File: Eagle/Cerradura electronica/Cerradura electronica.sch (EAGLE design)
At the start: 37 parts, among them IC1 LD117AS50TR, Q1 2N3904, Q2 IRF540N

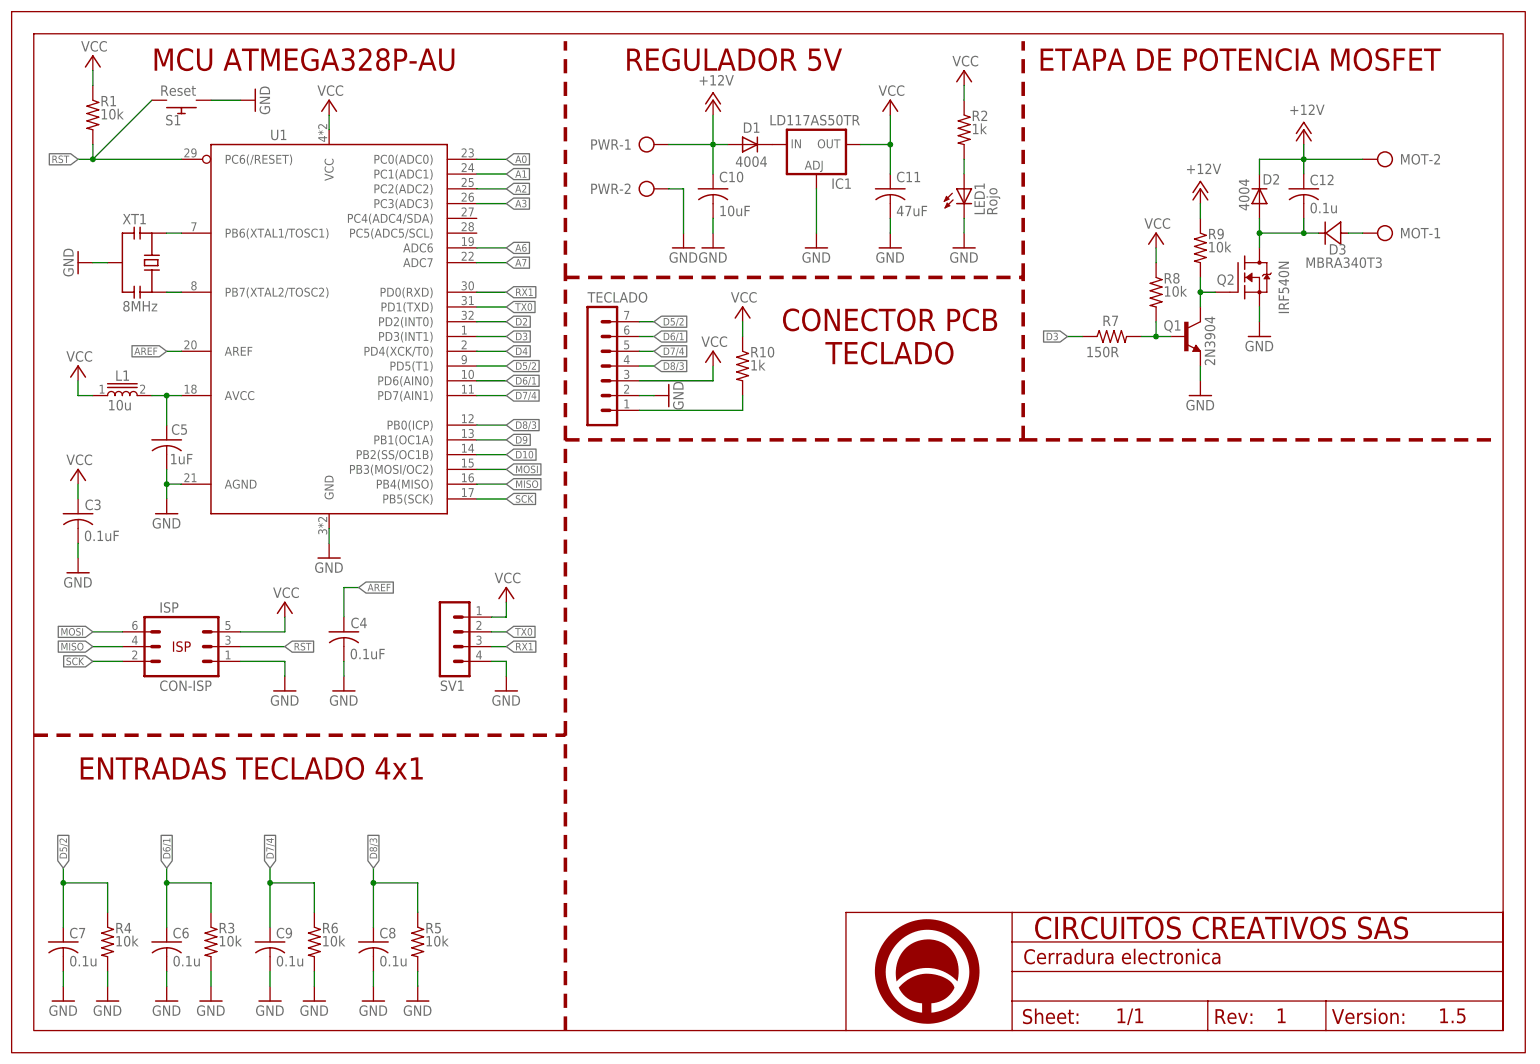
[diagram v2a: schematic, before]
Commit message: Add BUZZER para mejorar la funcionalidad, terminado v1.5.1
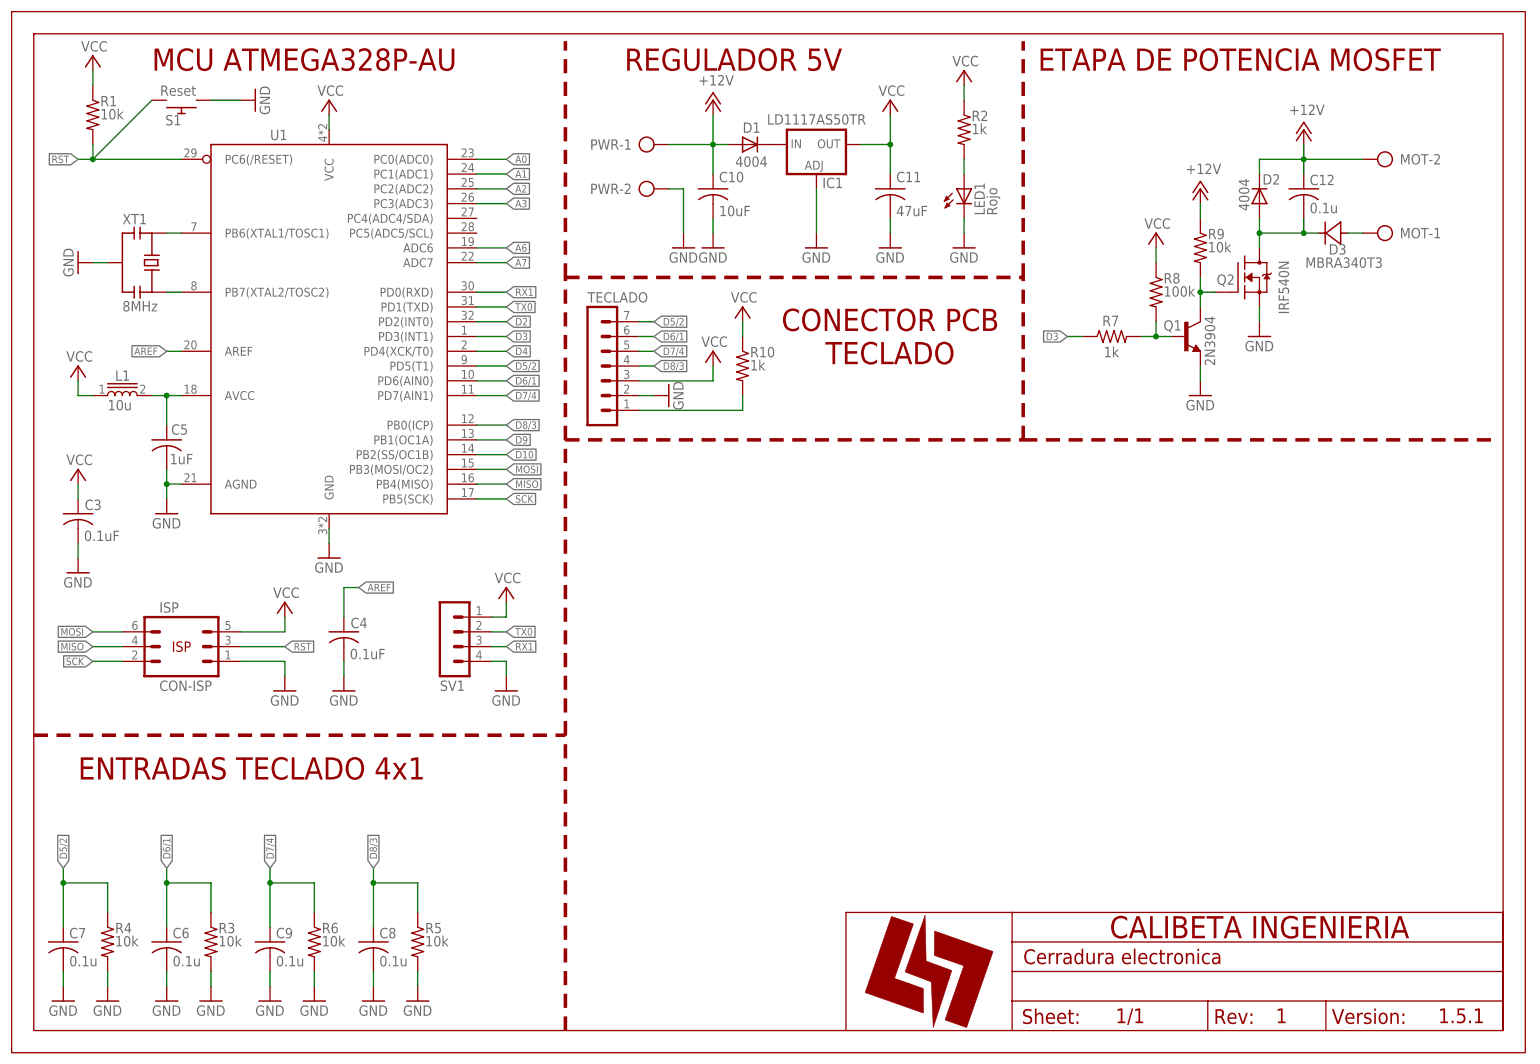
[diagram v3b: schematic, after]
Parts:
- IC1: value LD117AS50TR -> LD1117AS50TR; device v-reg:LD117AS50TR -> CaliBeta-IC power:LD1117AS50TR
- R7: value 150R -> 1k
- R8: value 10k -> 100k
- U$1: value A4_HORIZONTAL -> A4_H-LOGO; device Circuitos-Creativos-Estilos:A4_HORIZONTAL -> CaliBeta-Estilos:A4_H-LOGO
- XT1: device CaliBeta-Miselaneos:XTAL-CSTCE -> CaliBeta-Cristales:CSTNE8M00G52-R0
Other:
- note added: "1.5.1"
- note removed: "1.5"
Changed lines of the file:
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@@
 <part name="P+4" library="supply1" library_urn="urn:adsk.eagle:library:371" deviceset="VCC" device=""/>
 <part name="R1" library="CaliBeta-RCL" library_urn="urn:adsk.eagle:library:14345719" deviceset="RESISTOR_" device="R0805" package3d_urn="urn:adsk.eagle:package:14345749/1" value="10k"/>
-<part name="SV1" library="con-lstb" library_urn="urn:adsk.eagle:library:162" deviceset="MA04-1" device="" package3d_urn="urn:adsk.eagle:package:8337/1"/>
+<part name="SV1" library="con-lstb" library_urn="urn:adsk.eagle:library:162" deviceset="MA04-1" device="" package3d_urn="urn:adsk.eagle:package:8337/1" override_package3d_urn="urn:adsk.eagle:package:14744829/2" override_package_urn="urn:adsk.eagle:footprint:8285/1"/>
 <part name="P+19" library="supply1" library_urn="urn:adsk.eagle:library:371" deviceset="VCC" device=""/>
 <part name="GND22" library="SparkFun" deviceset="GND" device=""/>
@@
 <part name="C5" library="CaliBeta-RCL" library_urn="urn:adsk.eagle:library:14345719" deviceset="CAP" device="C0805" package3d_urn="urn:adsk.eagle:package:14345754/1" value="1uF"/>
 <part name="GND32" library="SparkFun" deviceset="GND" device=""/>
-<part name="U$1" library="Circuitos-Creativos-Estilos" deviceset="A4_HORIZONTAL" device=""/>
+<part name="U$1" library="CaliBeta-Estilos" deviceset="A4_H-LOGO" device=""/>
 <part name="Q1" library="CaliBeta-Transistores" library_urn="urn:adsk.eagle:library:14361247" deviceset="SS8050" device="" package3d_urn="urn:adsk.eagle:package:14361264/3" value="2N3904"/>
 <part name="LED1" library="CaliBeta-Diodos" library_urn="urn:adsk.eagle:library:14345451" deviceset="LED-ROJO" device="0805" package3d_urn="urn:adsk.eagle:package:14345485/2" value="Rojo"/>
 <part name="GND13" library="supply1" library_urn="urn:adsk.eagle:library:371" deviceset="GND" device=""/>
 <part name="P+14" library="supply1" library_urn="urn:adsk.eagle:library:371" deviceset="VCC" device=""/>
-<part name="IC1" library="v-reg" library_urn="urn:adsk.eagle:library:409" deviceset="LD117A?*" device="S" package3d_urn="urn:adsk.eagle:package:30370/1" technology="50TR" value="LD117AS50TR"/>
+<part name="IC1" library="CaliBeta-IC power" library_urn="urn:adsk.eagle:library:14742817" deviceset="LD1117A?*" device="S" package3d_urn="urn:adsk.eagle:package:14742823/2" technology="50TR" value="LD1117AS50TR"/>
 <part name="GND14" library="supply1" library_urn="urn:adsk.eagle:library:371" deviceset="GND" device=""/>
 <part name="C10" library="CaliBeta-RCL" library_urn="urn:adsk.eagle:library:14345719" deviceset="CAP" device="C1206" package3d_urn="urn:adsk.eagle:package:14345750/1" value="10uF"/>
@@
 <part name="R2" library="CaliBeta-RCL" library_urn="urn:adsk.eagle:library:14345719" deviceset="RESISTOR_" device="R0805" package3d_urn="urn:adsk.eagle:package:14345749/1" value="1k"/>
 <part name="PWR" library="CaliBeta-Conectores" library_urn="urn:adsk.eagle:library:14344905" deviceset="AK500-2" device="" package3d_urn="urn:adsk.eagle:package:14344939/2"/>
-<part name="R7" library="CaliBeta-RCL" library_urn="urn:adsk.eagle:library:14345719" deviceset="RESISTOR_" device="R0805" package3d_urn="urn:adsk.eagle:package:14345749/1" value="150R"/>
-<part name="R8" library="CaliBeta-RCL" library_urn="urn:adsk.eagle:library:14345719" deviceset="RESISTOR_" device="R0805" package3d_urn="urn:adsk.eagle:package:14345749/1" value="10k"/>
+<part name="R7" library="CaliBeta-RCL" library_urn="urn:adsk.eagle:library:14345719" deviceset="RESISTOR_" device="R0805" package3d_urn="urn:adsk.eagle:package:14345749/1" value="1k"/>
+<part name="R8" library="CaliBeta-RCL" library_urn="urn:adsk.eagle:library:14345719" deviceset="RESISTOR_" device="R0805" package3d_urn="urn:adsk.eagle:package:14345749/1" value="100k"/>
 <part name="P+1" library="supply1" library_urn="urn:adsk.eagle:library:371" deviceset="VCC" device=""/>
 <part name="D1" library="CaliBeta-Diodos" library_urn="urn:adsk.eagle:library:14345451" deviceset="DIODO" device="-DO-214AC" package3d_urn="urn:adsk.eagle:package:14345492/2" value="4004"/>
@@
 <part name="MOT" library="CaliBeta-Conectores" library_urn="urn:adsk.eagle:library:14344905" deviceset="AK500-2" device="" package3d_urn="urn:adsk.eagle:package:14344939/2"/>
 <part name="P+3" library="supply1" library_urn="urn:adsk.eagle:library:371" deviceset="+12V" device=""/>
-<part name="TECLADO" library="con-lstb" library_urn="urn:adsk.eagle:library:162" deviceset="MA07-1" device="" package3d_urn="urn:adsk.eagle:package:8341/1"/>
+<part name="TECLADO" library="con-lstb" library_urn="urn:adsk.eagle:library:162" deviceset="MA07-1" device="" package3d_urn="urn:adsk.eagle:package:8341/1" override_package3d_urn="urn:adsk.eagle:package:14744917/2" override_package_urn="urn:adsk.eagle:footprint:8291/1"/>
 <part name="R10" library="CaliBeta-RCL" library_urn="urn:adsk.eagle:library:14345719" deviceset="RESISTOR_" device="R0805" package3d_urn="urn:adsk.eagle:package:14345749/1" value="1k"/>
 <part name="P+6" library="supply1" library_urn="urn:adsk.eagle:library:371" deviceset="VCC" device=""/>
@@
 <part name="P+7" library="supply1" library_urn="urn:adsk.eagle:library:371" deviceset="VCC" device=""/>
 <part name="GND12" library="SparkFun" deviceset="GND" device=""/>
-<part name="XT1" library="CaliBeta-Miselaneos" library_urn="urn:adsk.eagle:library:14357685" deviceset="XTAL-" device="CSTCE" package3d_urn="urn:adsk.eagle:package:14357744/2" value="8MHz"/>
+<part name="XT1" library="CaliBeta-Cristales" library_urn="urn:adsk.eagle:library:14744356" deviceset="CSTNE8M00G52-R0" device="" package3d_urn="urn:adsk.eagle:package:14744359/3" value="8MHz"/>
 <part name="GND11" library="SparkFun" deviceset="GND" device=""/>
 </parts>
@@
 <text x="20.32" y="165.1" size="3.81" layer="94" ratio="10">MCU ATMEGA328P-AU</text>
 <text x="213.614" y="1.27" size="2.54" layer="94" ratio="10">1</text>
-<text x="241.554" y="1.27" size="2.54" layer="94" ratio="10">1.5</text>
+<text x="241.554" y="1.27" size="2.54" layer="94" ratio="10">1.5.1</text>
 <text x="7.62" y="43.18" size="3.81" layer="94" ratio="10">ENTRADAS TECLADO 4x1</text>
 <text x="101.6" y="165.1" size="3.81" layer="94" ratio="10">REGULADOR 5V</text>
@@
 <attribute name="VALUE" x="162.56" y="167.64" size="1.778" layer="96" ratio="10" rot="R180"/>
 </instance>
-<instance part="IC1" gate="G$1" x="134.62" y="152.4" smashed="yes">
-<attribute name="NAME" x="137.16" y="144.78" size="1.778" layer="95" ratio="10"/>
-<attribute name="VALUE" x="126.492" y="155.702" size="1.778" layer="96" ratio="10"/>
+<instance part="IC1" gate="G$1" x="134.62" y="149.86" smashed="yes">
+<attribute name="NAME" x="137.414" y="145.796" size="1.778" layer="95" ratio="10" align="center"/>
+<attribute name="VALUE" x="134.62" y="156.718" size="1.778" layer="96" ratio="10" align="center"/>
 </instance>
 <instance part="GND14" gate="1" x="111.76" y="134.62" smashed="yes">
@@
 packages will not be understood (or retained) with this version.
 </note>
+<note version="9.4" severity="warning">
+Since Version 9.4, EAGLE supports the overriding of 3D packages
+in schematics and board files. Those overridden 3d packages
+will not be understood (or retained) with this version.
+</note>
 </compatibility>
